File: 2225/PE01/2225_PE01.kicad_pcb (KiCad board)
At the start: 2 copper layers, 200 x 60 mm, 95 parts

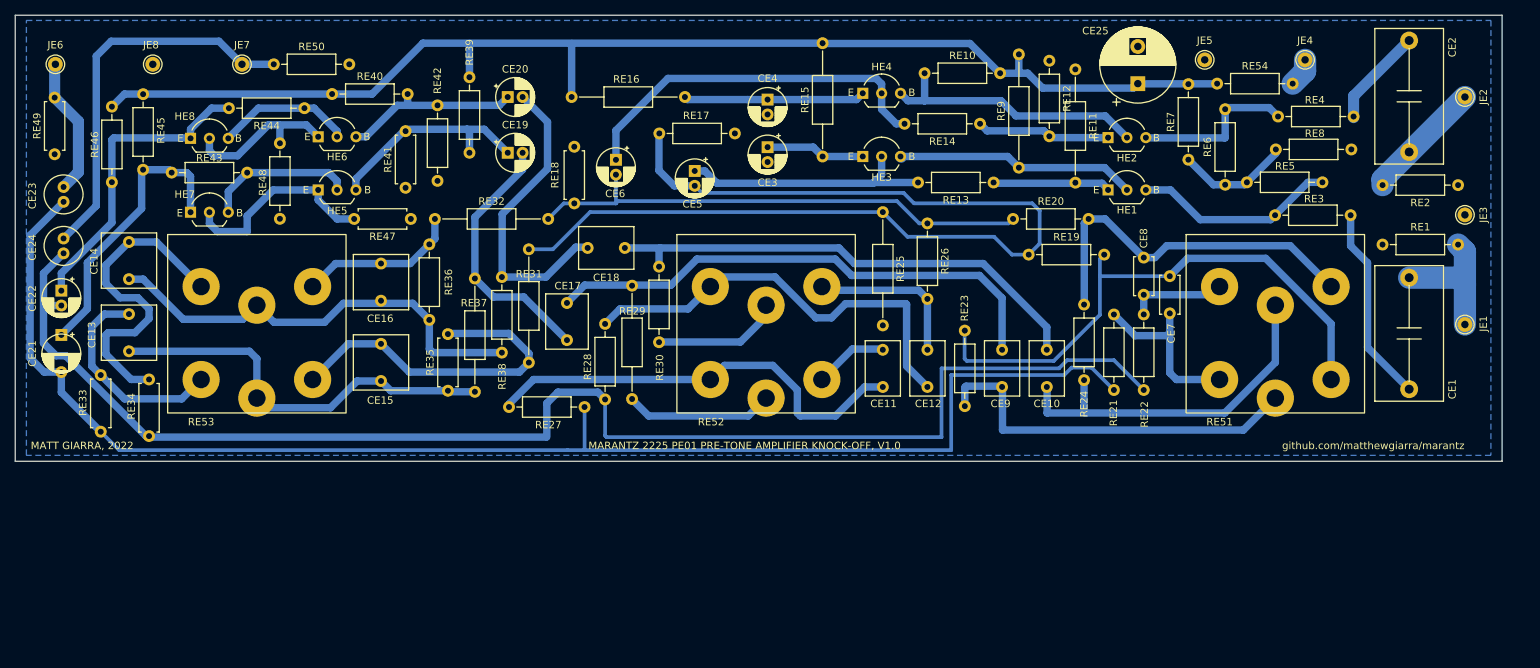
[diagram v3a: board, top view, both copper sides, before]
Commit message: Moved components and updated fooprints to mitigate design rules checker warnings
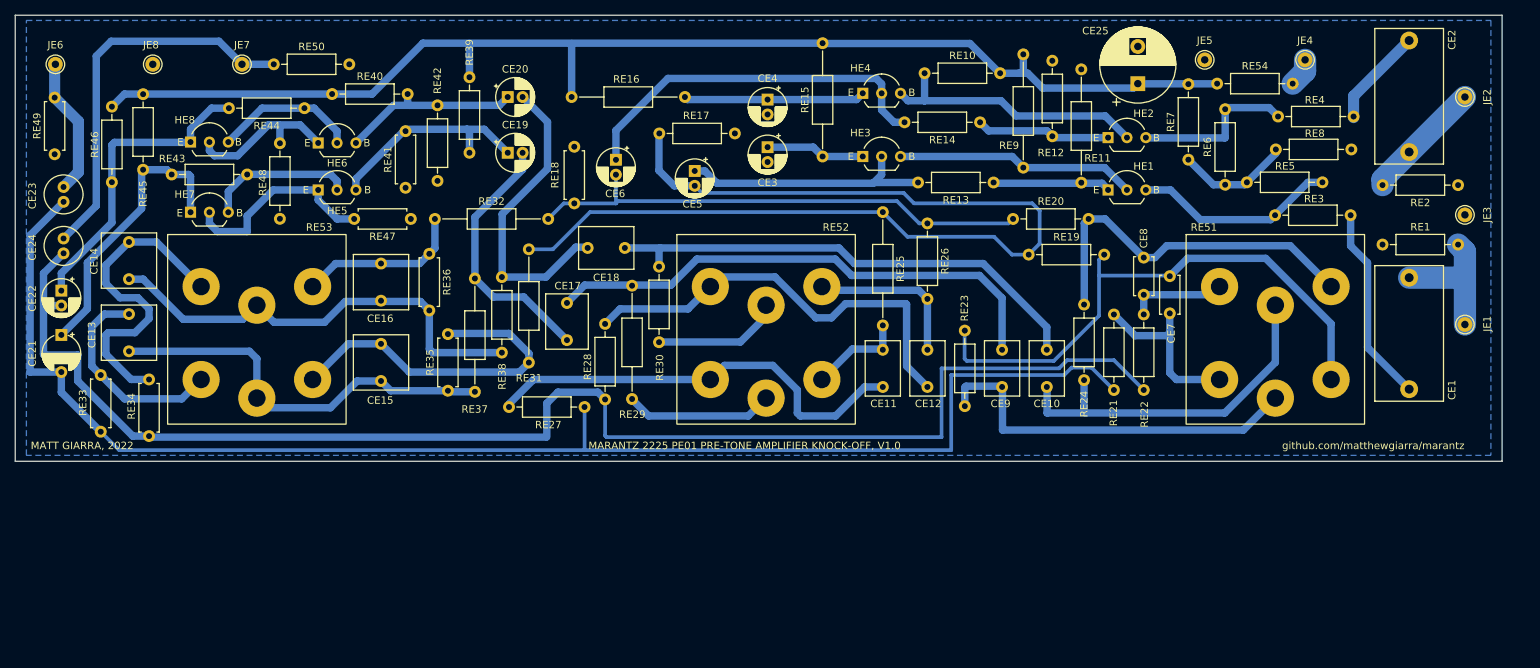
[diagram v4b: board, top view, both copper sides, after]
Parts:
- CE1, CE2: footprint Capacitor_THT:C_US_Rect_L18.0mm_W9.0mm_P15.00mm_FKS3_FKP3 -> Capacitor_THT:C_Rect_L18.0mm_W9.0mm_P15.00mm_FKS3_FKP3
- RE36: footprint Resistor_THT:R_Axial_DIN0207_L6.3mm_D2.5mm_P10.16mm_Horizontal -> Resistor_THT:R_Axial_DIN0207_L6.3mm_D2.5mm_P7.62mm_Horizontal
- moved RE36 1.27 mm to (55.7, 32.1)
- moved HE6 0.84 mm to (40.8, 17.2)
- moved RE11 0.80 mm to (143.4, 7.28)
- moved RE9 0.60 mm to (135.6, 20.5)
- moved HE8 0.50 mm to (23.6, 17.1)
- moved RE12 0.40 mm to (139.5, 6.12)
- moved RE43 0.25 mm to (31.2, 21.4)
- moved RE14 0.20 mm to (129.8, 14.4)
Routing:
- net Net-(RE52-Pad3): track 9.94 -> 13.2 mm
- net Net-(CE22-Pad2): track 190.5 -> 193.4 mm
- net Net-(CE21-Pad2): track 192.9 -> 194.1 mm
- net Net-(HE6-Pad2): track 18.4 -> 19.4 mm
- net Net-(RE53-Pad5): track 60.1 -> 61.0 mm
- net Net-(RE53-Pad4): track 21.8 -> 22.5 mm

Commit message: Changed and re-positioned pot footprints. Left traces as-is, so this commit is a WIP.
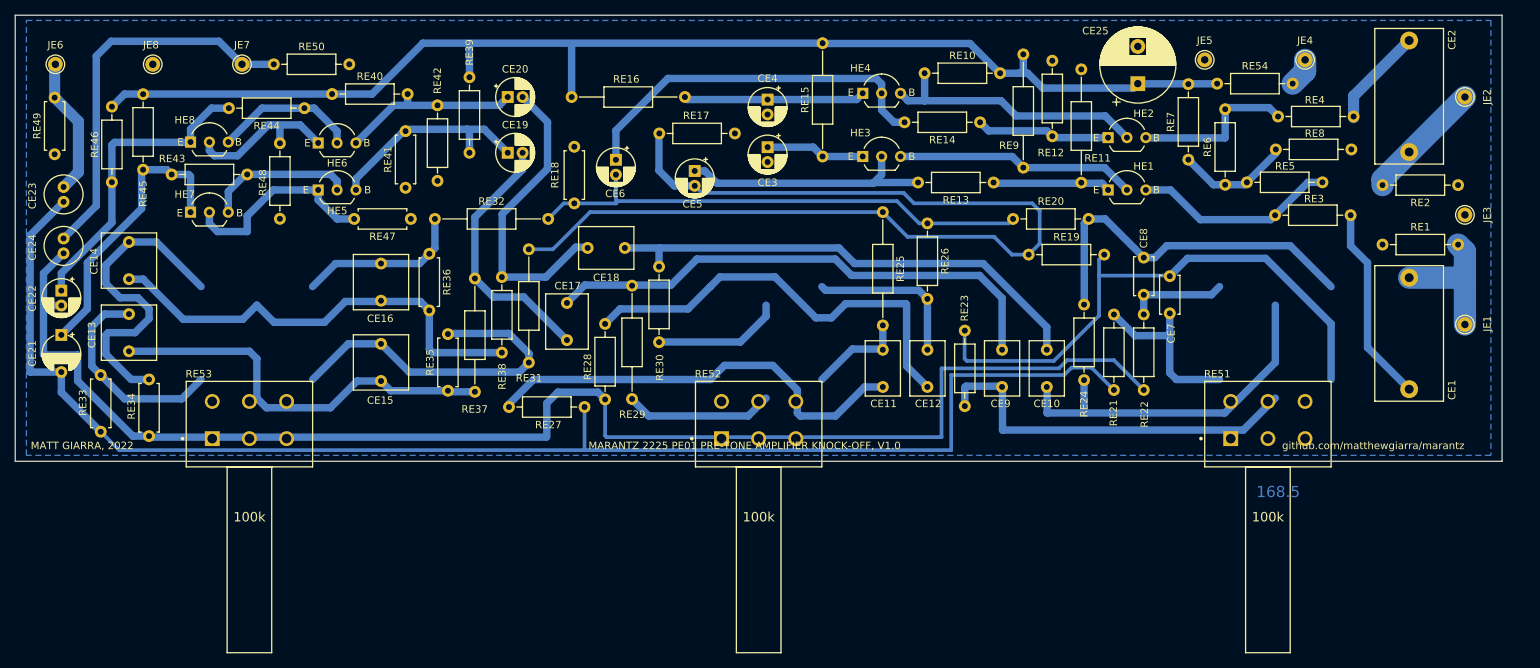
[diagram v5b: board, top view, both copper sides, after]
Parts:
- RE51, RE52, RE53: footprint Potentiometer_THT:Potentiometer_Marantz_RM0104005 -> Potentiometer_THT:Bourns-PDB182-K425K-103A
- moved RE51 19.6 mm to (168.5, 67.5)
- moved RE52 19.6 mm to (100.0, 67.5)
- moved RE53 19.6 mm to (31.5, 67.5)
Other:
- board text added: "100"
- board text added: "168.5"
- board text added: "31.5"

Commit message: Made board 4 layers and re-routed all the traces.
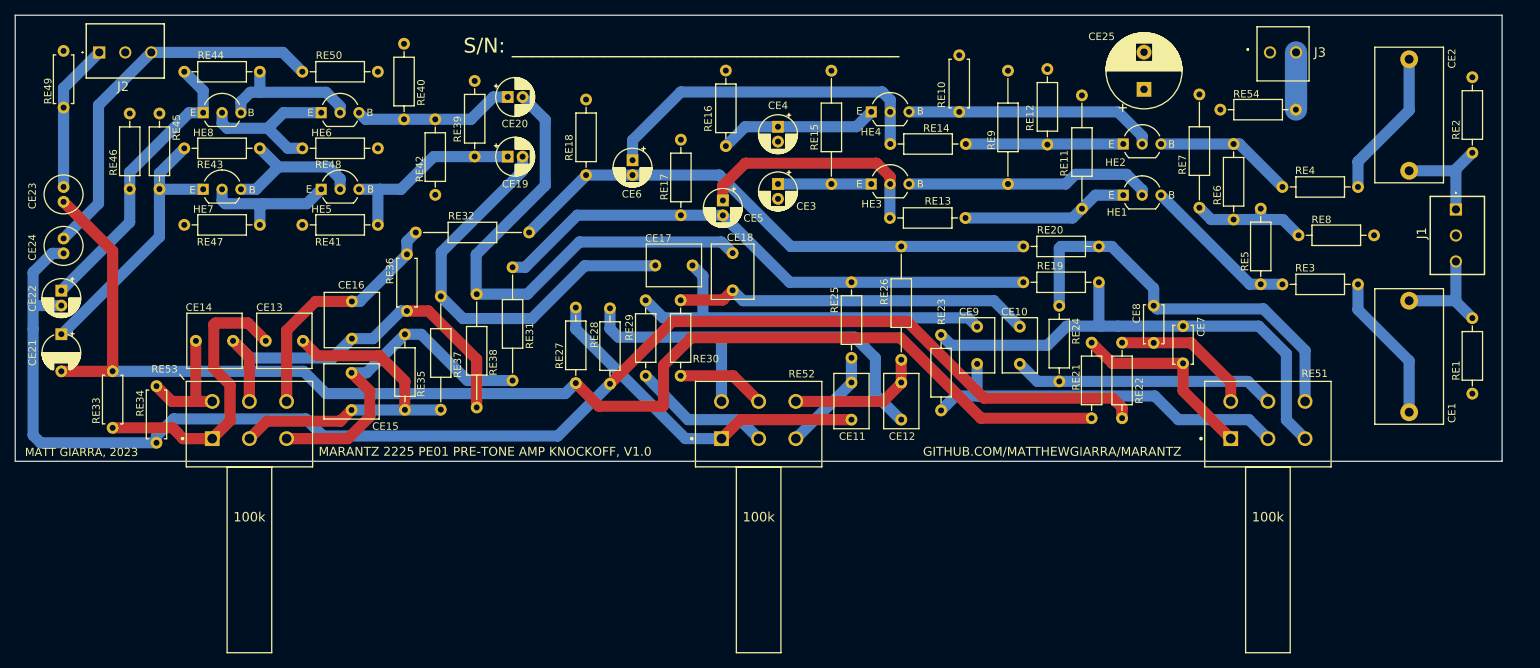
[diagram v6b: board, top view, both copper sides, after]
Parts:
- removed JE1, JE2, JE3, JE4, JE5, JE6, JE7, JE8: Conn_01x01_Male, Connector_Pin:Pin_D1.0mm_L10.0mm
- added J1: Screw_Terminal_01x03, Connector_Molex:Molex_Eurostyle_39357-0003_1x03_P3.5mm_Horizontal, F.Cu at (193.8, 26.1)
- added J2: Screw_Terminal_01x03, Connector_Molex:Molex_Eurostyle_39357-0003_1x03_P3.5mm_Horizontal, F.Cu at (11.3, 5.00)
- added J3: Screw_Terminal_01x02, Connector_Molex:Molex_Eurostyle_39357-0002_1x02_P3.5mm_Horizontal, F.Cu at (168.8, 5.00)
- CE1, CE2: value 0.22 µF -> 0.22u
- CE10, CE9: value 0.22 µF -> 2200p
- CE11, CE12: value 6800pF -> 6800p
- CE13, CE14, CE15, CE16: value 2200pF -> 0.022u
- CE17, CE18: value 0.01µF -> 0.01u
- CE19, CE20, CE23, CE24: value 1µF -> 1u
- CE21, CE22: value 33µF -> 3.3u
- CE25: value 220µF -> 220u
- CE3, CE4: value 10µF -> 10u
- CE5, CE6: value 4.7µF -> 4.7u
- CE7, CE8: value 100pF -> 100p
- HE1, HE2, HE5, HE6: value 2SC1941 -> KSC1845FTA
- HE3, HE4, HE7, HE8: value 2SA1015 -> KSA992FTA
- RE10: footprint Resistor_THT:R_Axial_DIN0207_L6.3mm_D2.5mm_P10.16mm_Horizontal -> Resistor_THT:R_Axial_DIN0207_L6.3mm_D2.5mm_P7.62mm_Horizontal
- RE16, RE25, RE29: footprint Resistor_THT:R_Axial_DIN0207_L6.3mm_D2.5mm_P15.24mm_Horizontal -> Resistor_THT:R_Axial_DIN0207_L6.3mm_D2.5mm_P10.16mm_Horizontal
- RE18, RE35, RE41, RE47: footprint Resistor_THT:R_Axial_DIN0207_L6.3mm_D2.5mm_P7.62mm_Horizontal -> Resistor_THT:R_Axial_DIN0207_L6.3mm_D2.5mm_P10.16mm_Horizontal
- RE26, RE38, RE7: footprint Resistor_THT:R_Axial_DIN0207_L6.3mm_D2.5mm_P10.16mm_Horizontal -> Resistor_THT:R_Axial_DIN0207_L6.3mm_D2.5mm_P15.24mm_Horizontal
- RE39, RE40: value 2.2M -> 2.2meg
- RE5, RE6: value 1M -> 1meg
- moved RE47 30.5 mm to (22.7, 28.2), turned to 0 degrees
- moved RE1 23.4 mm to (196.0, 50.9), turned to 90 degrees
- moved CE13 18.7 mm to (33.7, 43.8), turned to 0 degrees
- moved CE17 17.6 mm to (91.1, 33.6), turned to 180 degrees
- moved RE27 16.1 mm to (75.4, 39.3), turned to -90 degrees
- moved CE14 16.1 mm to (24.3, 43.8), turned to 0 degrees
- moved CE18 15.6 mm to (96.5, 37.0), turned to 90 degrees
- moved RE41 14.7 mm to (38.6, 28.2), turned to 0 degrees
- moved RE2 14.6 mm to (196.0, 8.34), turned to -90 degrees
- moved RE49 14.0 mm to (6.50, 4.80), turned to -90 degrees
- moved RE8 11.9 mm to (182.8, 29.6)
- moved RE40 11.8 mm to (52.3, 3.84), turned to -90 degrees
- moved RE25 10.3 mm to (112.5, 35.9)
- moved RE4 9.49 mm to (180.6, 23.1)
- moved RE3 9.35 mm to (180.6, 36.2)
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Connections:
- net Ground renamed GND
- net Net-(CE1-Pad1) renamed Vin_L
- net Net-(CE19-Pad1) renamed /HE5_B
- net Net-(CE2-Pad1) renamed Vin_R
- net Net-(CE23-Pad2) renamed Vout_L
- net Net-(CE24-Pad2) renamed Vout_R
- net Net-(CE25-Pad1) renamed /pwr
- net Net-(CE3-Pad1) renamed /HE3_E
- net Net-(CE5-Pad1) renamed /HE3_C
- net Net-(HE1-Pad1) renamed /HE1_E
- net Net-(HE1-Pad2) renamed /HE1_C
- net Net-(HE1-Pad3) renamed /HE1_B
- RE54 pad 2: Net-(JE4-Pad1) -> Vcc
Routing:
- net /pwr: track 169.4 -> 0.00 mm
- net Net-(CE5-Pad2): track 136.6 -> 75.3 mm
- net Net-(CE18-Pad2): track 41.4 -> 69.7 mm
- net Net-(CE14-Pad1): track 44.1 -> 16.6 mm
- net Net-(CE17-Pad2): track 35.4 -> 56.4 mm
- net Net-(CE10-Pad2): track 66.6 -> 48.2 mm
- net Net-(CE17-Pad1): track 70.1 -> 53.7 mm
- net Net-(CE21-Pad2): track 194.1 -> 178.6 mm
- net Net-(CE10-Pad1): track 49.2 -> 35.5 mm
- net Net-(CE11-Pad1): track 59.1 -> 47.0 mm
- net Net-(CE16-Pad2): track 22.5 -> 33.4 mm
- net Net-(CE13-Pad1): track 28.6 -> 39.3 mm
- net Net-(HE5-Pad1): track 27.4 -> 18.9 mm
- net Net-(CE7-Pad2): track 76.3 -> 68.1 mm
- net Net-(CE13-Pad2): track 54.9 -> 47.2 mm
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- added copper zone on In1.Cu, net /pwr
- added copper zone on In2.Cu, net GND
- removed copper zone on B.Cu, net GND
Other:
- copper layers 2 -> 4
- board text added: "GITHUB.COM/MATTHEWGIARRA/MARANTZ"
- board text added: "MARANTZ 2225 PE01 PRE-TONE AMP KNOCKOFF, V1.0"
- board text added: "MATT GIARRA, 2023"
- board text added: "S/N: ______________________________________"
- board text removed: "168.5"
- board text removed: "MARANTZ 2225 PE01 PRE-TONE AMPLIFIER KNOCK-OFF, V1.0"
- board text removed: "MATT GIARRA, 2022"
- board text removed: "github.com/matthewgiarra/marantz"

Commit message: Updated design rules and some footprints to match EasyEDA requirements.
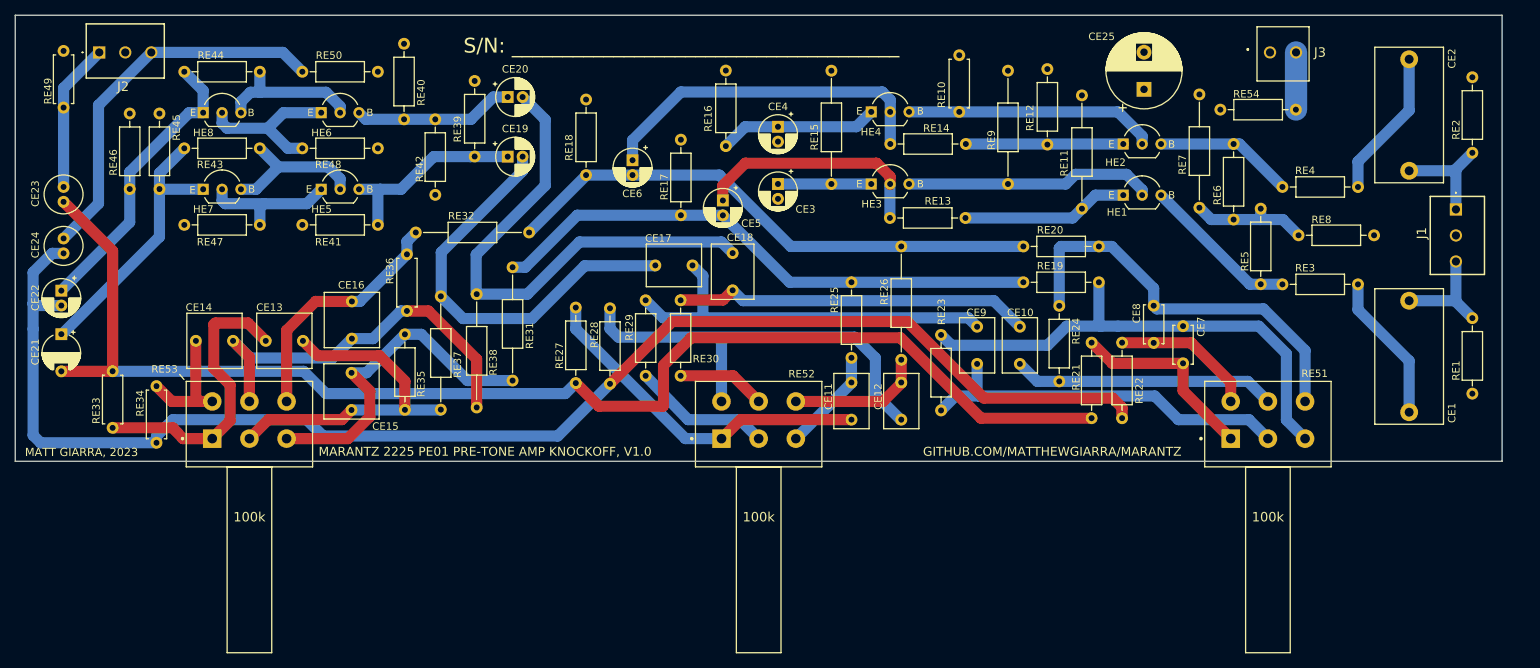
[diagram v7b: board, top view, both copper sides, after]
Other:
- rule pad_to_mask_clearance: 0 -> 0.2

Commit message: Cropped footprints that overlapped board edge; moved some text.
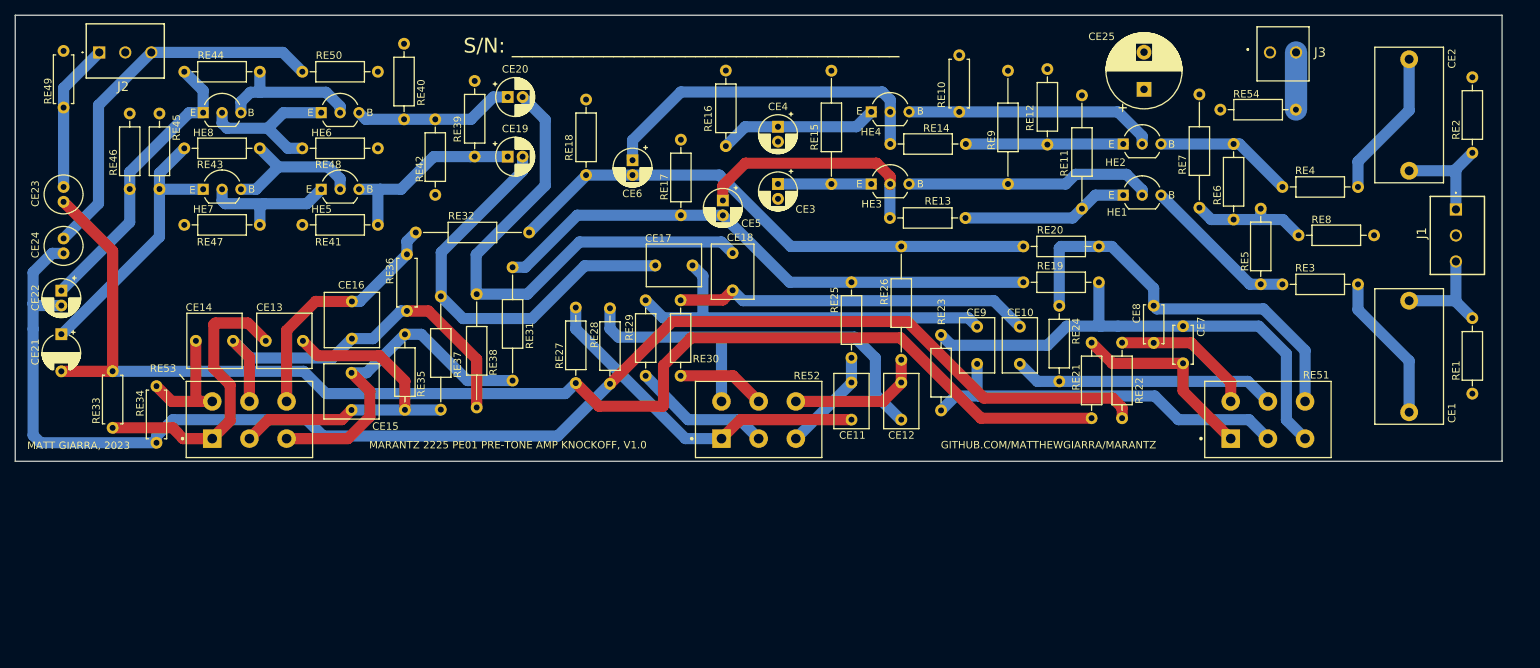
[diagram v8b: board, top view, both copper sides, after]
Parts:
- RE51, RE52, RE53: footprint Potentiometer_THT:Bourns-PDB182-K425K-103A -> Potentiometer_THT:Bourns-PDB182-K425K-103A_cropped
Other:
- rule pad_to_mask_clearance: 0.2 -> 0
